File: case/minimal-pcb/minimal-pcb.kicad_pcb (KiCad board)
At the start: 2 copper layers, 60 x 65 mm, 8 parts, among them J1 USB_C_Receptacle_USB2.0

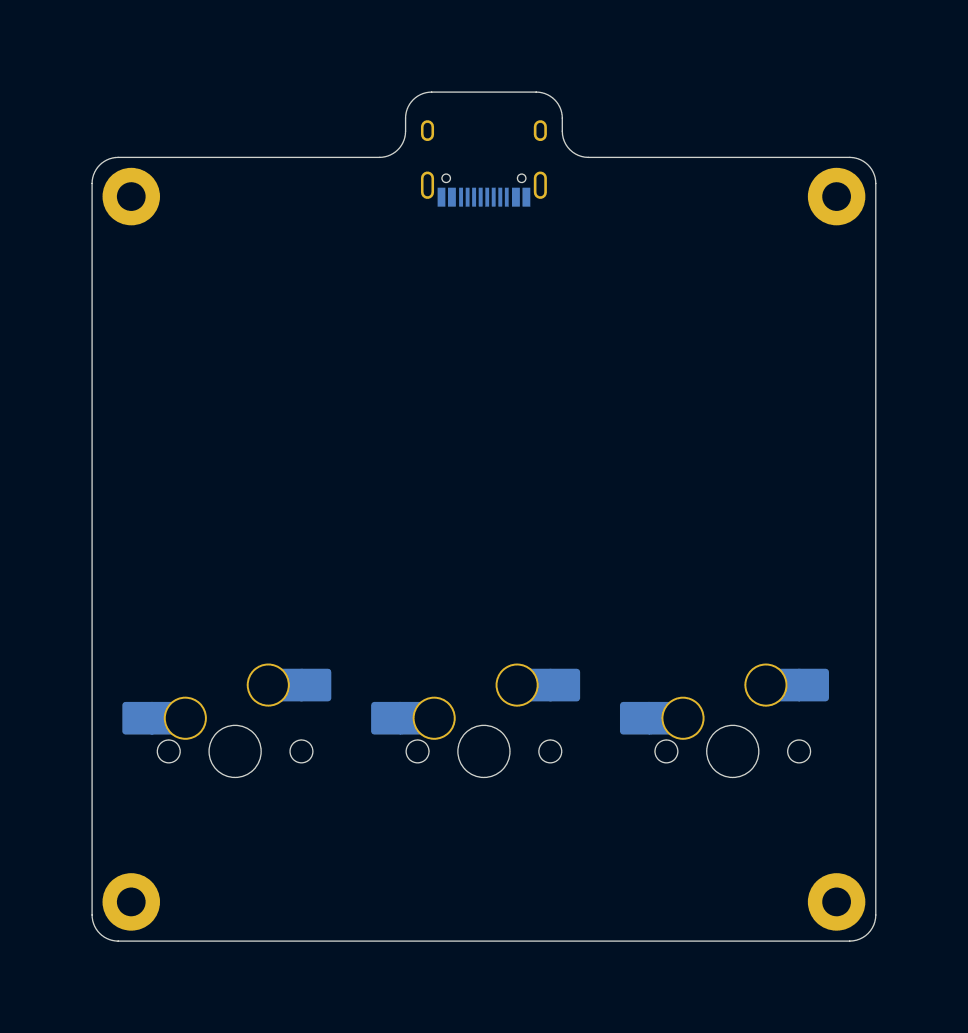
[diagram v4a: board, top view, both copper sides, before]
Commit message: fix: use 70x70mm pcb size and 80x80mm case
proides enough clearance all of the parts, as I've already managed to route traces this way.
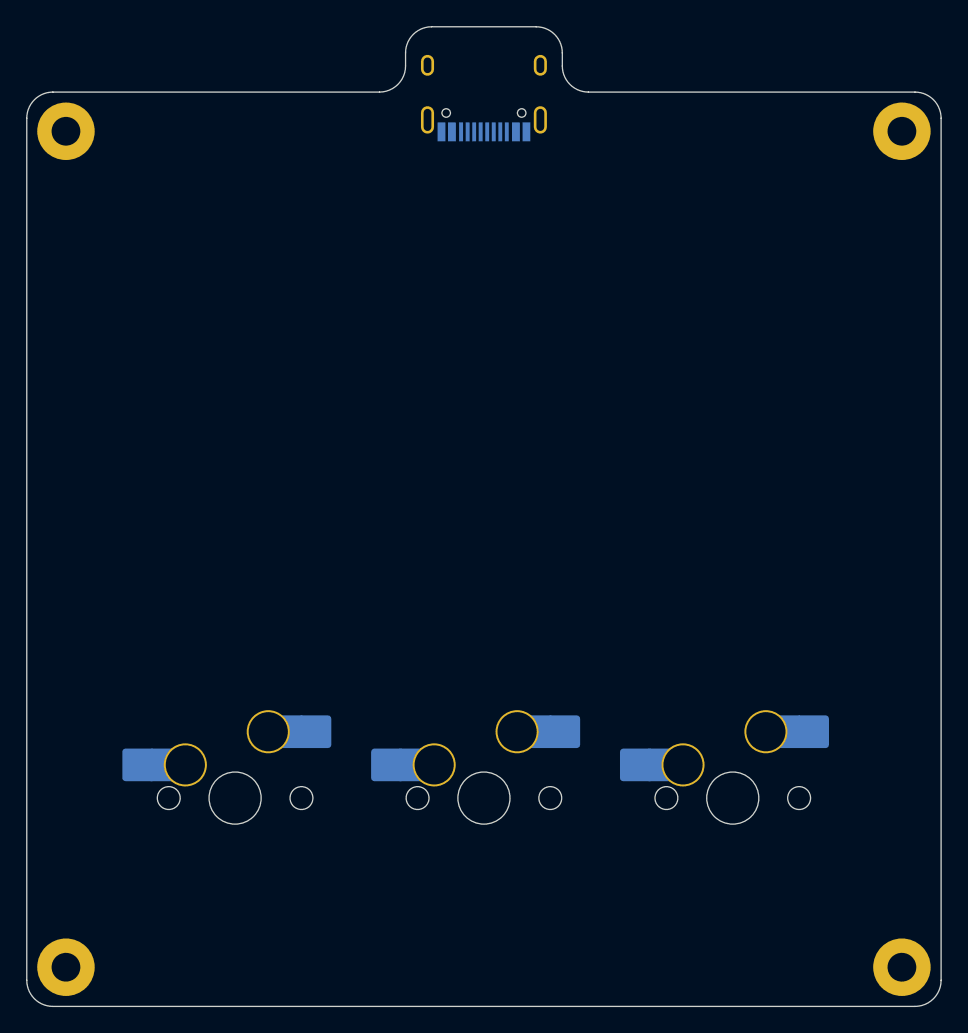
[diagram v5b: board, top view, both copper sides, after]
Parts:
- moved H1 7.07 mm to (25.1, 24.8)
- moved H2 7.07 mm to (89.2, 24.8)
- moved H3 7.07 mm to (25.1, 88.8)
- moved H4 7.07 mm to (89.2, 88.8)
- moved J1 5.00 mm to (57.1, 20.8)
- moved MX1 3.57 mm to (76.2, 75.8)
- moved MX2 3.57 mm to (57.1, 75.8)
- moved MX3 3.57 mm to (38.1, 75.8)
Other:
- board size 60 x 65 mm -> 70 x 75 mm
- board text added: "70x70mm PCB 5mm extension at top of PCB for USB-C port Switches 19.05mm below centre of PCB M2 mounting holes 3mm away from edge"
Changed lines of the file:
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@@
   (net 17 "unconnected-(J1-SHIELD-PadS1)")
   (footprint "PCM_marbastlib-mx:SW_MX_HS_1u" (layer "B.Cu")
-    (at 38.099984 72.239785 180)
+    (at 38.099984 75.811647 180)
     (descr "Footprint for Cherry MX style switches with Kailh hotswap socket")
     (property "Sheetfile" "minimal-pcb.kicad_sch")
@@
   )
   (footprint "PCM_marbastlib-mx:SW_MX_HS_1u" (layer "B.Cu")
-    (at 57.15 72.239785 180)
+    (at 57.15 75.811647 180)
     (descr "Footprint for Cherry MX style switches with Kailh hotswap socket")
     (property "Sheetfile" "minimal-pcb.kicad_sch")
@@
   )
   (footprint "PCM_marbastlib-mx:SW_MX_HS_1u" (layer "B.Cu")
-    (at 76.200016 72.239785 180)
+    (at 76.200016 75.811647 180)
     (descr "Footprint for Cherry MX style switches with Kailh hotswap socket")
     (property "Sheetfile" "minimal-pcb.kicad_sch")
@@
   )
   (footprint "MountingHole:MountingHole_2.2mm_M2_Pad" (layer "B.Cu")
-    (at 84.15 29.761647 180)
+    (at 89.15 24.761647 180)
     (descr "Mounting Hole 2.2mm, M2")
     (tags "mounting hole 2.2mm m2")
@@
   )
   (footprint "MountingHole:MountingHole_2.2mm_M2_Pad" (layer "B.Cu")
-    (at 84.15 83.761647 180)
+    (at 89.15 88.761647 180)
     (descr "Mounting Hole 2.2mm, M2")
     (tags "mounting hole 2.2mm m2")
@@
   )
   (footprint "MountingHole:MountingHole_2.2mm_M2_Pad" (layer "B.Cu")
-    (at 30.15 83.761647 180)
+    (at 25.15 88.761647 180)
     (descr "Mounting Hole 2.2mm, M2")
     (tags "mounting hole 2.2mm m2")
@@
   )
   (footprint "MountingHole:MountingHole_2.2mm_M2_Pad" (layer "B.Cu")
-    (at 30.15 29.761647 180)
+    (at 25.15 24.761647 180)
     (descr "Mounting Hole 2.2mm, M2")
     (tags "mounting hole 2.2mm m2")
@@
   )
   (footprint "PCM_marbastlib-various:USB_C_Receptacle_HRO_TYPE-C-31-M-12" (layer "B.Cu")
-    (at 57.15 25.761647)
+    (at 57.15 20.761647)
     (descr "USB Type-C receptacle for USB 2.0 and PD, http://www.krhro.com/uploads/soft/180320/1-1P320120243.pdf")
     (tags "usb usb-c 2.0 pd")
@@
     )
   )
-  (gr_arc (start 51.15 23.761647) (mid 51.735786 22.347433) (end 53.15 21.761647)
-    (stroke (width 0.1) (type default)) (layer "Edge.Cuts"))
-  (gr_line (start 51.15 23.761647) (end 51.15 24.761647)
-    (stroke (width 0.1) (type default)) (layer "Edge.Cuts"))
-  (gr_line (start 61.15 21.761647) (end 53.15 21.761647)
-    (stroke (width 0.1) (type default)) (layer "Edge.Cuts"))
-  (gr_arc (start 27.15 28.761647) (mid 27.735786 27.347433) (end 29.15 26.761647)
-    (stroke (width 0.1) (type default)) (layer "Edge.Cuts"))
-  (gr_arc (start 87.15 84.761647) (mid 86.564197 86.17583) (end 85.15 86.761647)
-    (stroke (width 0.1) (type default)) (layer "Edge.Cuts"))
-  (gr_line (start 63.15 24.761647) (end 63.15 23.761647)
-    (stroke (width 0.1) (type default)) (layer "Edge.Cuts"))
-  (gr_arc (start 29.15 86.761647) (mid 27.735786 86.175861) (end 27.15 84.761647)
-    (stroke (width 0.1) (type default)) (layer "Edge.Cuts"))
-  (gr_line (start 85.15 86.761647) (end 29.15 86.761647)
-    (stroke (width 0.1) (type default)) (layer "Edge.Cuts"))
-  (gr_arc (start 85.15 26.761647) (mid 86.564214 27.347433) (end 87.15 28.761647)
-    (stroke (width 0.1) (type default)) (layer "Edge.Cuts"))
-  (gr_line (start 65.15 26.761647) (end 85.15 26.761647)
-    (stroke (width 0.1) (type default)) (layer "Edge.Cuts"))
-  (gr_line (start 87.15 28.761647) (end 87.15 84.761647)
-    (stroke (width 0.1) (type default)) (layer "Edge.Cuts"))
-  (gr_line (start 27.15 84.761647) (end 27.15 28.761647)
-    (stroke (width 0.1) (type default)) (layer "Edge.Cuts"))
-  (gr_arc (start 61.15 21.761647) (mid 62.564215 22.347433) (end 63.15 23.761647)
-    (stroke (width 0.1) (type default)) (layer "Edge.Cuts"))
-  (gr_arc (start 65.15 26.761647) (mid 63.735787 26.17586) (end 63.15 24.761647)
-    (stroke (width 0.1) (type default)) (layer "Edge.Cuts"))
-  (gr_arc (start 51.15 24.761647) (mid 50.564214 26.175861) (end 49.15 26.761647)
-    (stroke (width 0.1) (type default)) (layer "Edge.Cuts"))
-  (gr_line (start 29.15 26.761647) (end 49.15 26.761647)
-    (stroke (width 0.1) (type default)) (layer "Edge.Cuts"))
+  (gr_line (start 24.15 21.761647) (end 49.15 21.761647)
+    (stroke (width 0.1) (type default)) (layer "Edge.Cuts"))
+  (gr_arc (start 92.15 89.761647) (mid 91.564197 91.17583) (end 90.15 91.761647)
+    (stroke (width 0.1) (type default)) (layer "Edge.Cuts"))
+  (gr_line (start 65.15 21.761647) (end 90.15 21.761647)
+    (stroke (width 0.1) (type default)) (layer "Edge.Cuts"))
+  (gr_line (start 63.15 18.761647) (end 63.15 19.761647)
+    (stroke (width 0.1) (type default)) (layer "Edge.Cuts"))
+  (gr_arc (start 51.15 19.761647) (mid 50.564197 21.17583) (end 49.15 21.761647)
+    (stroke (width 0.1) (type default)) (layer "Edge.Cuts"))
+  (gr_arc (start 22.15 23.761647) (mid 22.73577 22.347403) (end 24.15 21.761647)
+    (stroke (width 0.1) (type default)) (layer "Edge.Cuts"))
+  (gr_line (start 90.15 91.761647) (end 24.15 91.761647)
+    (stroke (width 0.1) (type default)) (layer "Edge.Cuts"))
+  (gr_arc (start 51.15 18.761647) (mid 51.73577 17.347403) (end 53.15 16.761647)
+    (stroke (width 0.1) (type default)) (layer "Edge.Cuts"))
+  (gr_arc (start 61.15 16.761647) (mid 62.564214 17.347433) (end 63.15 18.761647)
+    (stroke (width 0.1) (type default)) (layer "Edge.Cuts"))
+  (gr_line (start 22.15 89.761647) (end 22.15 23.761647)
+    (stroke (width 0.1) (type default)) (layer "Edge.Cuts"))
+  (gr_arc (start 24.15 91.761647) (mid 22.735786 91.175861) (end 22.15 89.761647)
+    (stroke (width 0.1) (type default)) (layer "Edge.Cuts"))
+  (gr_line (start 92.15 23.761647) (end 92.15 89.761647)
+    (stroke (width 0.1) (type default)) (layer "Edge.Cuts"))
+  (gr_line (start 53.15 16.761647) (end 61.15 16.761647)
+    (stroke (width 0.1) (type default)) (layer "Edge.Cuts"))
+  (gr_arc (start 65.15 21.761647) (mid 63.735786 21.175861) (end 63.15 19.761647)
+    (stroke (width 0.1) (type default)) (layer "Edge.Cuts"))
+  (gr_line (start 51.15 19.761647) (end 51.15 18.761647)
+    (stroke (width 0.1) (type default)) (layer "Edge.Cuts"))
+  (gr_arc (start 90.15 21.761647) (mid 91.564214 22.347433) (end 92.15 23.761647)
+    (stroke (width 0.1) (type default)) (layer "Edge.Cuts"))
+  (gr_text "70x70mm PCB\n5mm extension at top of PCB for USB-C port\nSwitches 19.05mm below centre of PCB\nM2 mounting holes 3mm away from edge" (at 97.15 27.761647) (layer "Cmts.User")
+    (effects (font (size 1 1) (thickness 0.15)) (justify left bottom))
+  )
 )
